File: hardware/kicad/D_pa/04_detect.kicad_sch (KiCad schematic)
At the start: 22 parts, among them J20 DPD -> C karti, J40 ANTEN -> panel SO-239, K20 G6K-2F-Y, T20 FT50-43 1:32, T21 FT50-43 1:32, U30 AD8318ACPZ, U31 AD8318ACPZ

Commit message: Connect the pads that had no net
A symbol pin number must agree with the footprint pad number. If the
numbers do not agree, the net goes nowhere. The netlist removes it
and gives no message. ERC examines the schematic and sees a wire. DRC
does not count an unconnected pad as a violation. All three boards
showed zero ERC violations while 31 pads had no net.

Two of these faults stopped a board.

The footprint of the Ethernet PHY was for a different part. The
project used QFN-48 6x6 mm with 0.4 mm pitch. The RTL8211F(I)-CG is
WQFN-40-EP 5x5 mm. You cannot solder the part to that pad pattern.

The 25 MHz crystal had a 2-pin symbol on a 4-pad footprint. On a 3225
crystal the terminals are the diagonal pads 1 and 3. Pads 2 and 4 are
the metal can. XO went to pad 2. There was no crystal between XI and
XO, and thus neither PHY could make a clock.

The paddle of the AD9251 was pin 0 in the symbol and pad 65 in the
footprint. The paddle of the PE4312 was Pad against pad 21. The gas
discharge tubes had one electrode unconnected, because
Device:GDT_2Pin uses pins 1 and 3 but the varistor footprint uses
pads 1 and 2. A local footprint with pads 1 and 3 corrects this.

ped_denetim.py finds these faults on the board. yap.sh runs it before
the DSN export. The chain stops if a pad has no net.

The DSN export also changed. It declared In1 and In4 as power layers
but did not export the copper on them. The router thus believed that
the two ground planes were empty. It routed the 289 pins of GND as
traces on the signal layers. The planes now go out as conduction
areas.
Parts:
- removed U30, U31: AD8318ACPZ, Package_DFN_QFN:NXP_VQFN-16-1EP_4x4mm_P0.65mm_EP2.1x2.1mm, symbol dogrudan-sdr:AD8318
- added U60, U61: AD8318ACPZ, Package_DFN_QFN:NXP_VQFN-16-1EP_4x4mm_P0.65mm_EP2.1x2.1mm, symbol dogrudan-sdr:AD8318
- R404, R408: value 61R9 -> 19R1
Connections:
- net +5V: now also U60.16 (ENBL), U60.3 (VPSI), U60.4 (VPSI2), U60.9 (VPSO), U61.16 (ENBL), U61.3 (VPSI), U61.4 (VPSI2), U61.9 (VPSO)
- net ANT_OUT: now also T21.3 (SA); no longer T21.1 (AA), T21.2 (AB)
- net FWD_CLPF: now also U60.5 (CLPF)
- net FWD_DET: now also U60.14 (INHI)
- net FWD_LOG: now also U60.6 (VOUT), U60.7 (VSET)
- net FWD_TADJ: now also U60.10 (TADJ)
- net GND: now also T21.2 (AB), U60.1 (CMIP), U60.11 (CMIP3), U60.12 (CMIP4), U60.15 (INLO), U60.17 (EPAD), U60.2 (CMIP2), U60.8 (CMOP), U61.1 (CMIP), U61.11 (CMIP3), U61.12 (CMIP4), U61.15 (INLO), U61.17 (EPAD), U61.2 (CMIP2), U61.8 (CMOP); no longer R400.2, R402.2, T20.4 (SB)
- net REV_CLPF: now also U61.5 (CLPF)
- net REV_DET: now also U61.14 (INHI)
- net REV_LOG: now also U61.6 (VOUT), U61.7 (VSET)
- net REV_RAW: now also T20.4 (SB); no longer T21.3 (SA)
- net REV_TADJ: now also U61.10 (TADJ)
- new net CPL_COM: R400.2, R402.2, T21.1 (AA)
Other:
- note added: "FT50-43 x2. T20: birincil 1 sarim (duz gecen tel), ikincil 32. T21: 32 sarim hat-toprak arasi, 1 sarim CPL_COM'a. Akim ornegi 51 x I/32, gerilim ornegi V/32. Toplam ileri porta, fark yansiyan porta gidiyor; 50 ohm yukte yansiyan port sifir. Bir onceki devrede REV yapisi geregi sifirdi — arasindaki fark, olcumun olup olmamasi. Kuplaj eski (tek trafolu, hatali) devreye gore 6 dB daha yuksek: iki or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"
- note added: "KUPLOR — tandem match, akim + gerilim ornegi"
- note added: "VSET cikisa bagli = OLCUM modu (kontrol modu degil). Cikis girise logaritmik: -25 mV/dB, 0 dBm'de ~0.5 V. Giris araligi -60..0 dBm, yani 60 dB. Tandem kuplor + sont zayiflatici birlikte ~-50 dB: 100 W'ta detektor ~0 dBm goruyor, 100 mW'ta -30 dBm. Butun guc merdiveni araligin icinde. Kesin degeri devreye almada kukla yukle olculecek; log detektorun kalibrasyonu zaten olcumle yapiliyor. PINOUT VER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"
- note removed: "FT50-43, birincil 1 sarim (duz gecen tel), ikincil 32 sarim. -30 dB kuplaj: 100 W'ta orneklenen 100 mW = +20 dBm. AD8318'in girisi -60..0 dBm; araya 20 dB zayiflatici gerekiyor, asagida. YONLULUK sarimin duzgunlugune bagli: ikincil cekirdege ESIT aralikli ve tam sarilmali. 20 dB yonluluk yeterli ve dikkatli sarimla cikiyor; ozensiz sarimda 10 dB'ye duser ve SWR olcumu yaniltir — koruma yanlis and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"
- note removed: "KUPLOR — ikili toroid, -30 dB"
- note removed: "VSET cikisa bagli = OLCUM modu (kontrol modu degil). Cikis girise logaritmik: -25 mV/dB, 0 dBm'de ~0.5 V. Giris araligi -60..0 dBm, yani 60 dB. Kuplor -30 dB, araya 20 dB zayiflatici: 100 W'ta detektor 0 dBm goruyor, 100 mW'ta -30 dBm. Butun guc merdiveni araligin icinde. PINOUT VERI SAYFASINDAN (Rev.E Tablo 3) — ilk cizimde tahmin etmis ve isaretlemistim; dokuz bacagin HICBIRI tutmadi. Isaretlem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"

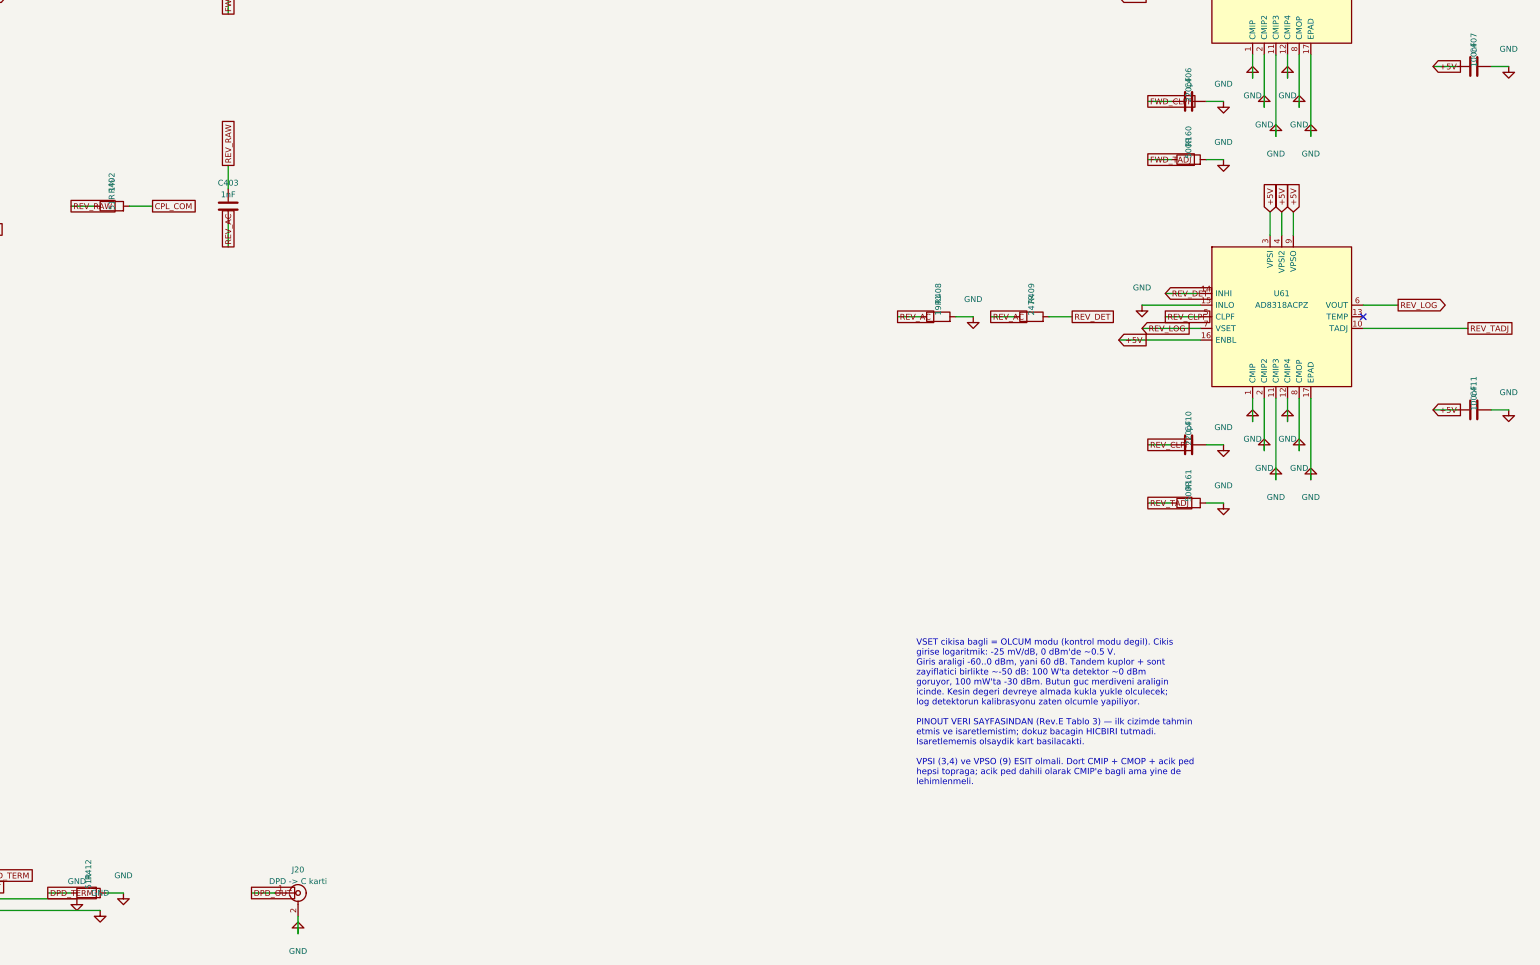
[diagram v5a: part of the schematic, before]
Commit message: Move each decoupling capacitor to the pin it serves
The audit found 14 chips with no decoupling capacitor within 15 mm.
Across the boards the nearest capacitor to a supply rail was a median
7.5 mm on A and 6.3 mm on C, and 91 mm in the worst case. A capacitor
45 mm from its pin has about 45 nH of loop inductance, near 2.8 ohm at
10 MHz, where milliohms are necessary. It is on the schematic, it is
in the BOM, it is fitted, and it does nothing.

The pass that moves capacitors ran before the fallback placer, so a
chip with no explicit rule was not yet placed and never entered the
pool. The fallback then gave every spare capacitor to the chip with
the most pins on the rail, which is the FPGA on +3V3. Small parts got
none. The pass now runs last.

A count of missing parts was also wrong. Every pad on a rail was
counted as a supply pin, including logic inputs tied high: SRCLR on
the 74HC595, SLEEP on the DRV8833, P/S on the PE4312. Counting only
pins the netlist marks power_in, board C has 15 supply pins and 15
capacitors. Four capacitors are missing across all three boards, not
59. The AD8318 has three supply pins and had one capacitor; it now
has three. The ADCLK846 has six and had five.
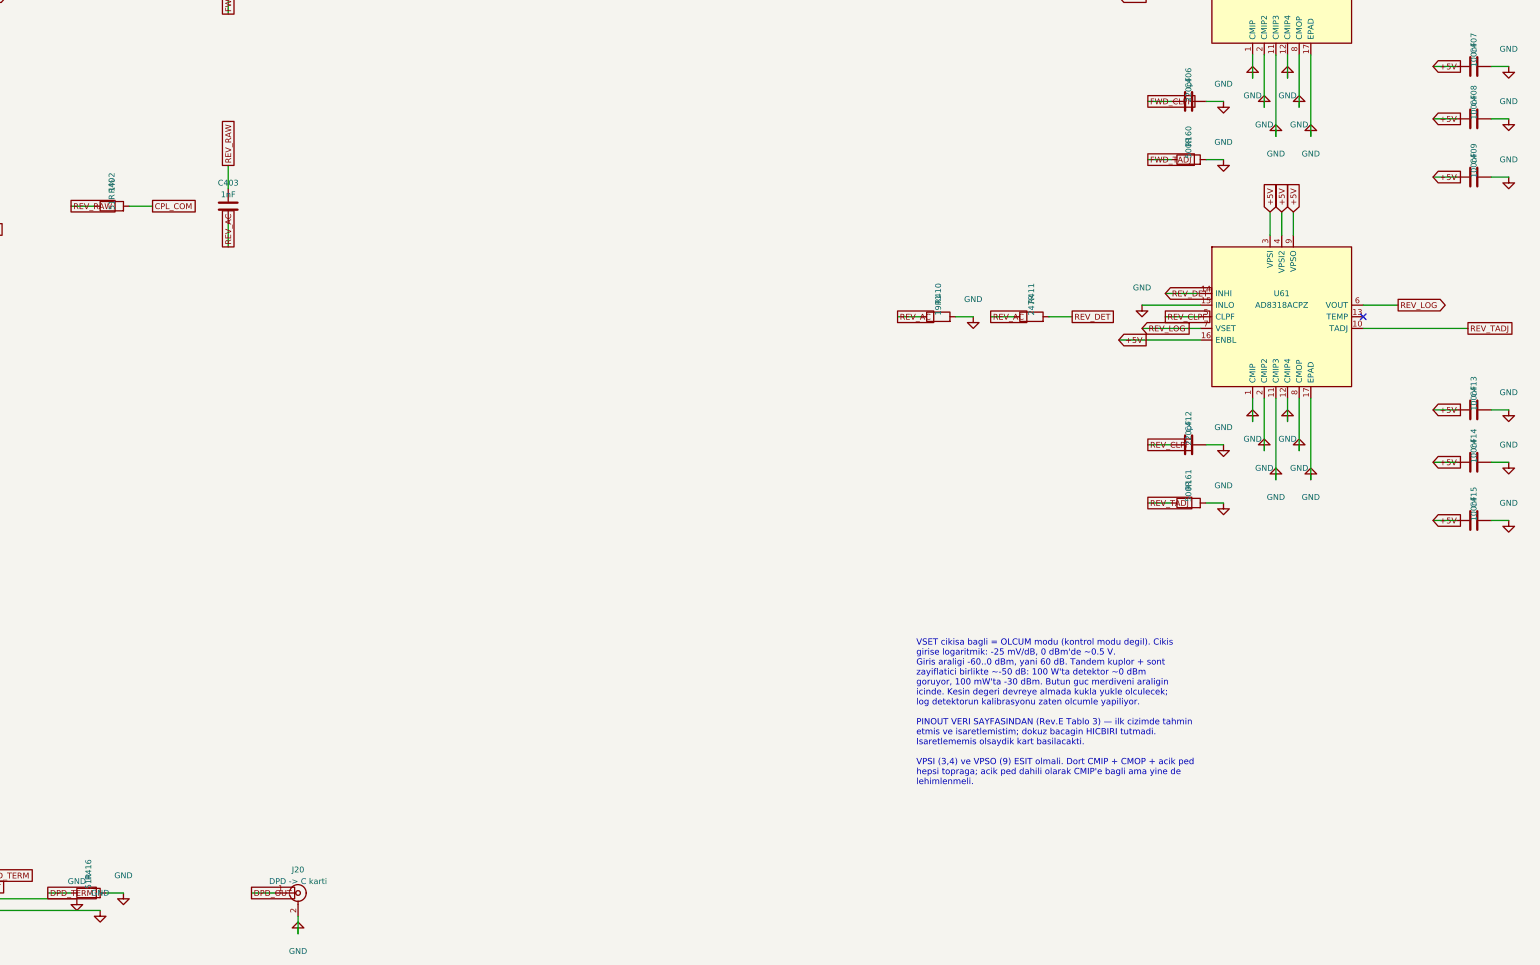
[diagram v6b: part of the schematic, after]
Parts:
- removed C410: 220pF, Capacitor_SMD:C_0603_1608Metric, symbol Device:C
- removed C411: 100nF, Capacitor_SMD:C_0603_1608Metric, symbol Device:C
- removed R408: 19R1, Resistor_SMD:R_0603_1608Metric, symbol Device:R
- removed R409: 247R, Resistor_SMD:R_0603_1608Metric, symbol Device:R
- removed R412: 51R, Resistor_SMD:R_0603_1608Metric, symbol Device:R
- added C408, C409, C413, C414, C415: 100nF, Capacitor_SMD:C_0603_1608Metric, symbol Device:C
- added C412: 220pF, Capacitor_SMD:C_0603_1608Metric, symbol Device:C
- added R410: 19R1, Resistor_SMD:R_0603_1608Metric, symbol Device:R
- added R411: 247R, Resistor_SMD:R_0603_1608Metric, symbol Device:R
- added R416: 51R, Resistor_SMD:R_0603_1608Metric, symbol Device:R
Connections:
- net +5V: now also C408.1, C409.1, C413.1, C414.1, C415.1
- net DPD_TERM: now also R416.1
- net GND: now also C408.2, C409.2, C412.2, C413.2, C414.2, C415.2, R410.2, R416.2
- net REV_AC: now also R410.1, R411.1
- net REV_CLPF: now also C412.1
- net REV_DET: now also R411.2
